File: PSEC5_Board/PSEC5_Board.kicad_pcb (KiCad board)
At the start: 6 copper layers, 76.2 x 76.2 mm, 187 parts, among them IC1 LTC6409IUDB#TRMPBF, IC2 LTC6409IUDB#TRMPBF, IC3 LTC6409IUDB#TRMPBF, IC4 LTC6409IUDB#TRMPBF, IC5 LTC6409IUDB#TRMPBF, IC6 LTC6409IUDB#TRMPBF, IC7 LTC6409IUDB#TRMPBF, IC8 LTC6409IUDB#TRMPBF, J1 QTH-040-01-X-D-DP-A, J11 Conn_Coaxial, J2 Conn_Coaxial, J3 Conn_Coaxial, J4 Conn_Coaxial, J5 Conn_Coaxial, J6 Conn_Coaxial, J7 Conn_Coaxial, J8 Conn_Coaxial, J9 QTH-040-01-X-D-DP-A, U1 MCP1700T-1802E_TT, U3 DAC8411IDCKT, U5 MC100LVEL, U6 OPA607QDBVRQ1, U7 AD4008BCPZ-RL7, Y1 ASE2-40.000MHZ-ET

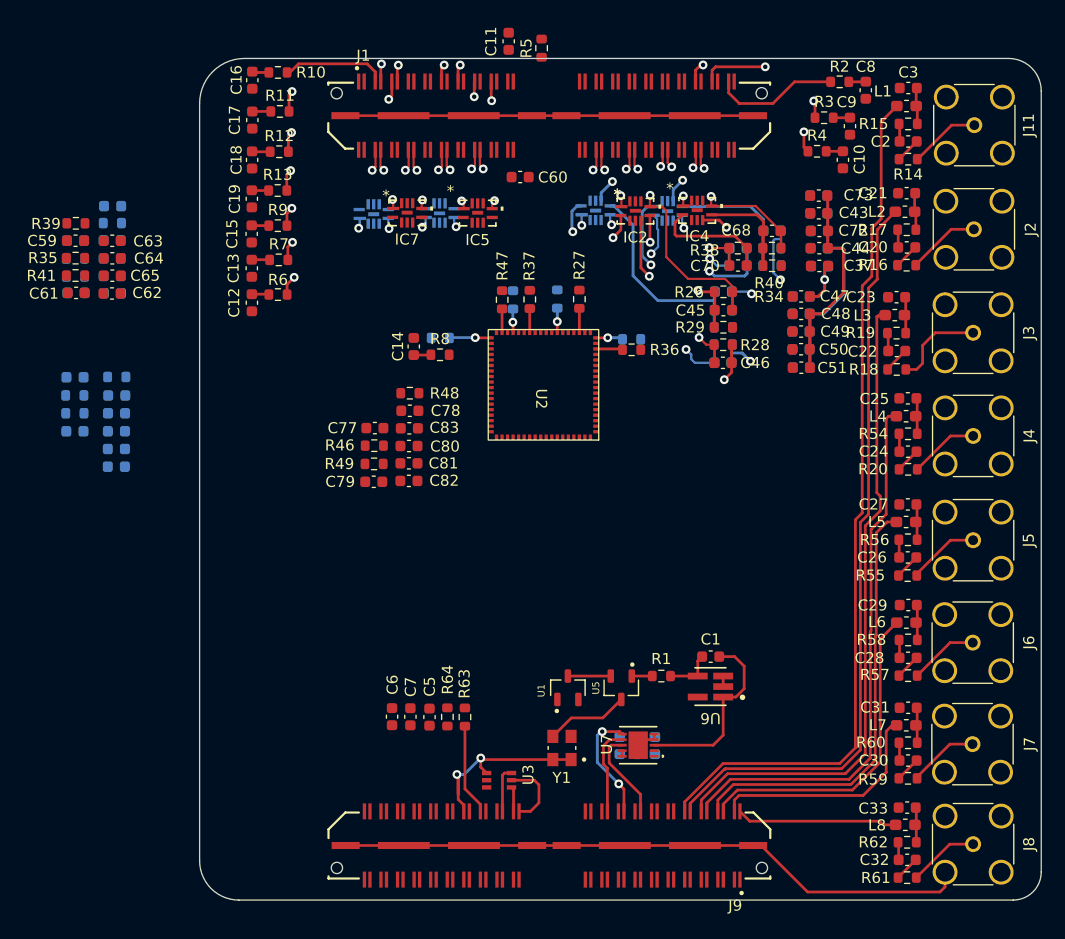
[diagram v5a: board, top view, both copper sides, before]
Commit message: DUT push - All nets
All nets are connected, Power and ground planes not registering.

ERC not completed.
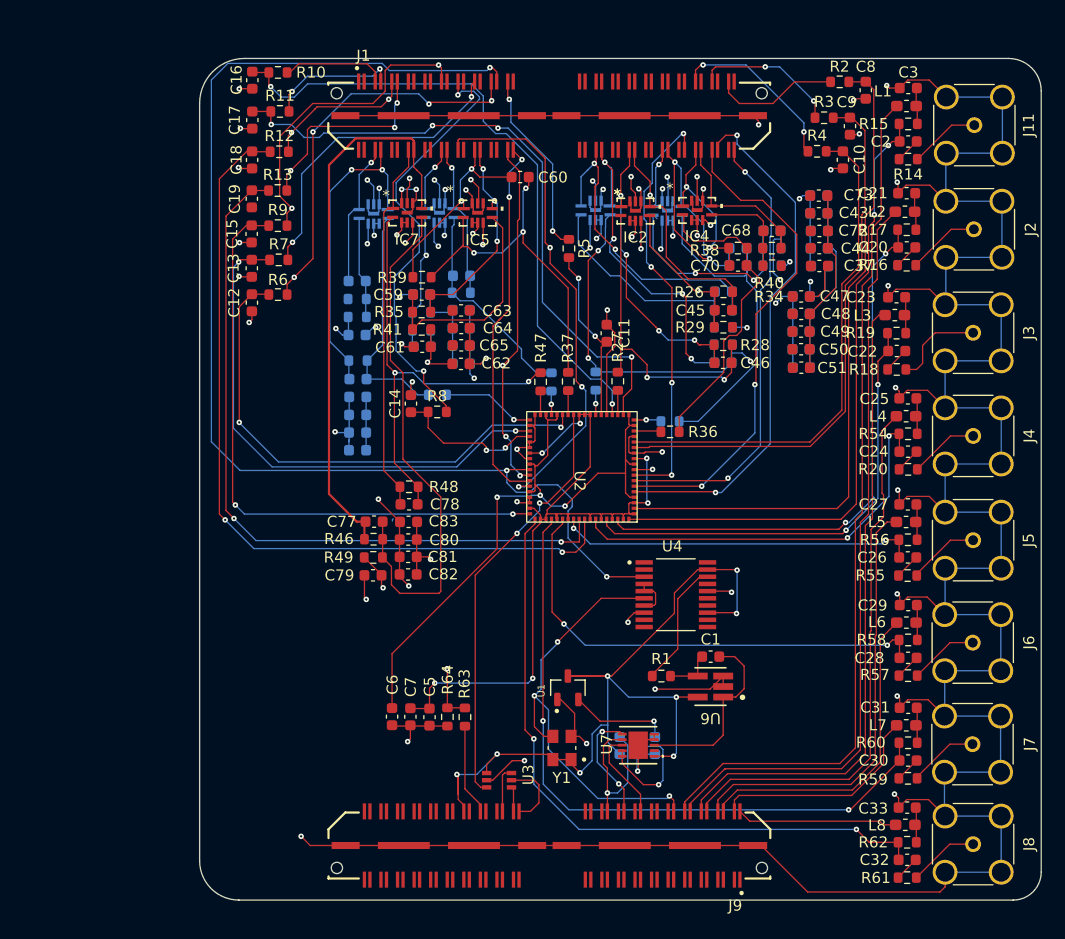
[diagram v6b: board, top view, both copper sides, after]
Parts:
- removed U5: MC100LVEL, MCP1700T_1802E_TT:SOT95P237X112-3N
- added U4: MC100LVEL40DWG, MC100LVEL40DWG:SOP65P640X120-20N, F.Cu at (158.1, 92.4)
- moved C62 32.2 mm to (138.6, 71.5)
- moved C71 32.2 mm to (138.6, 71.5)
- moved C63 32.2 mm to (138.6, 66.6)
- moved C64 32.2 mm to (138.6, 68.2)
- moved C65 32.2 mm to (138.6, 69.8)
- moved C67 32.2 mm to (138.7, 63.5)
- moved C74 32.2 mm to (138.6, 66.6)
- moved C75 32.2 mm to (138.6, 69.8)
- moved C76 32.2 mm to (138.6, 68.2)
- moved R44 32.2 mm to (138.6, 65.0)
- moved C61 31.7 mm to (135.1, 69.9)
- moved C66 31.7 mm to (135.1, 69.9)
- moved R45 31.7 mm to (135.0, 66.8)
- moved C69 31.7 mm to (135.0, 65.2)
- moved R42 31.7 mm to (135.0, 68.4)
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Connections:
- J1 pad 06: ADC8_Out+ -> ADC8_Out-
- J1 pad 08: ADC8_Out- -> ADC8_Out+
- J1 pad 22: ADC6_Out+ -> ADC6_Out-
- J1 pad 24: ADC6_Out- -> ADC6_Out+
- J1 pad 34: rst -> unconnected-(J1-Pad34)
- J1 pad 36: SPIclk -> unconnected-(J1-Pad36)
- J1 pad 46: ADC4_Out+ -> ADC4_Out-
- J1 pad 48: ADC4_Out- -> ADC4_Out+
- J1 pad 62: ADC2_Out+ -> ADC2_Out-
- J1 pad 64: ADC2_Out- -> ADC2_Out+
- J1 pad 74: unconnected-(J1-Pad74) -> rst
- J1 pad 76: unconnected-(J1-Pad76) -> SPIclk
- J9 pad 18: unconnected-(J9-Pad18) -> CLK_OUT
- Y1 pad 3: /Phase_detection/CLK_OUT -> CLK_OUT
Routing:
- net GND: track 97.6 -> 457.9 mm, vias 0 -> 50
- net PSEC5_CLK_OUT: track 0.00 -> 110.7 mm, vias 0 -> 3
- net /Biases,Thresh/wbufbias_postrc: track 1.65 -> 73.0 mm, vias 0 -> 2
- net +1V2: track 0.00 -> 68.6 mm, vias 0 -> 6
- net /Biases,Thresh/discbias_postrc: track 1.53 -> 66.7 mm, vias 0 -> 2
- net /Pedestals/SIGNAL8: track 1.61 -> 61.4 mm, vias 0 -> 2
- net /Pedestals/SIGNAL7: track 1.63 -> 61.0 mm, vias 0 -> 2
- net /Biases,Thresh/discthresh1_postrc: track 1.54 -> 60.2 mm
- net VDD25: track 23.4 -> 81.9 mm, vias 2 -> 8
- net +2V5: track 0.00 -> 57.2 mm, vias 0 -> 3
- net /Biases,Thresh/readbias1_postrc: track 1.53 -> 58.2 mm, vias 0 -> 2
- net /Biases,Thresh/readbias2_postrc: track 1.68 -> 58.0 mm, vias 0 -> 4
- net /Pedestals/SIGNAL1: track 1.61 -> 57.6 mm, vias 0 -> 2
- net VDD33: track 37.9 -> 92.9 mm, vias 0 -> 20
- net /Biases,Thresh/discthresh8_postrc: track 1.56 -> 54.9 mm, vias 0 -> 2
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- added copper zone on In1.Cu, net GND
- added copper zone on In4.Cu, net GND
- added copper zone on In2.Cu, net VDD33
- added copper zone on In3.Cu, net V_OCM

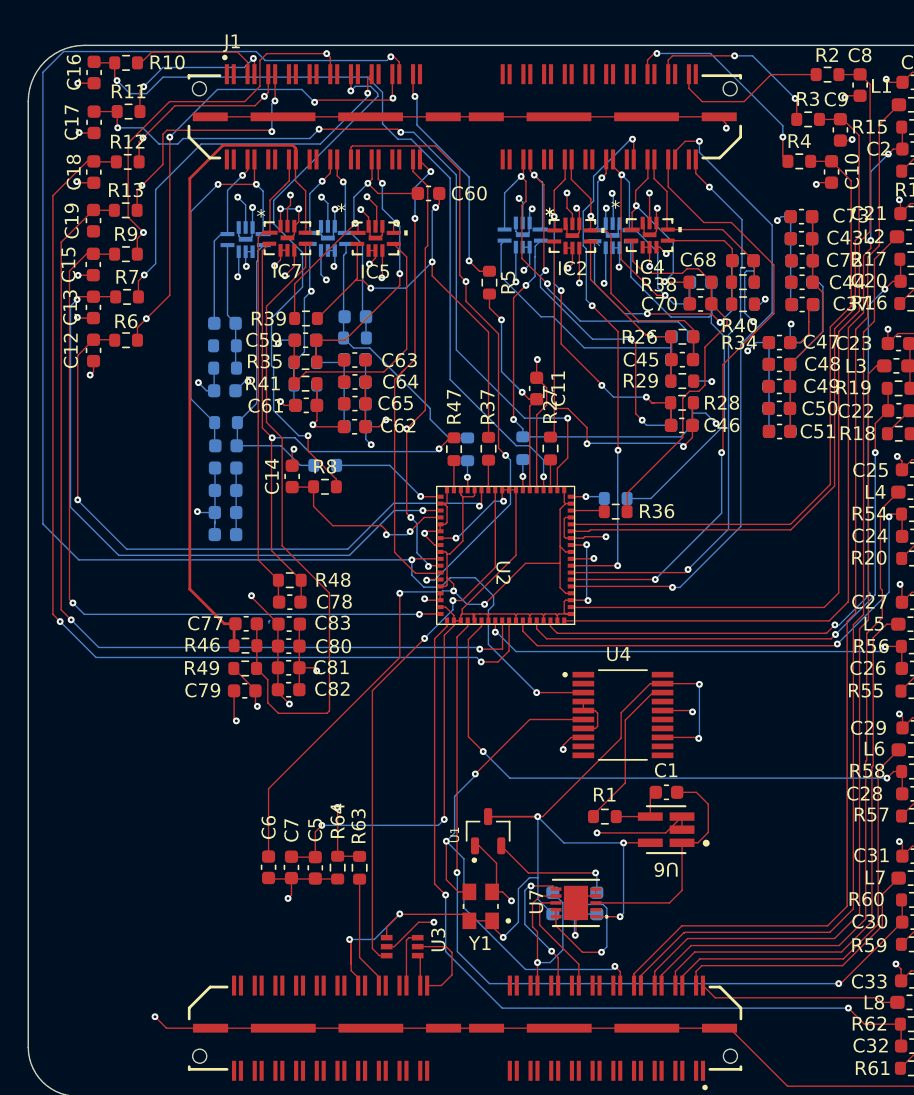
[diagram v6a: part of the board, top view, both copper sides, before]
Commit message: DUT - pre-review: Error free
Ran ERC, no more errors. Cleared most warnings besides silkscreen clipping
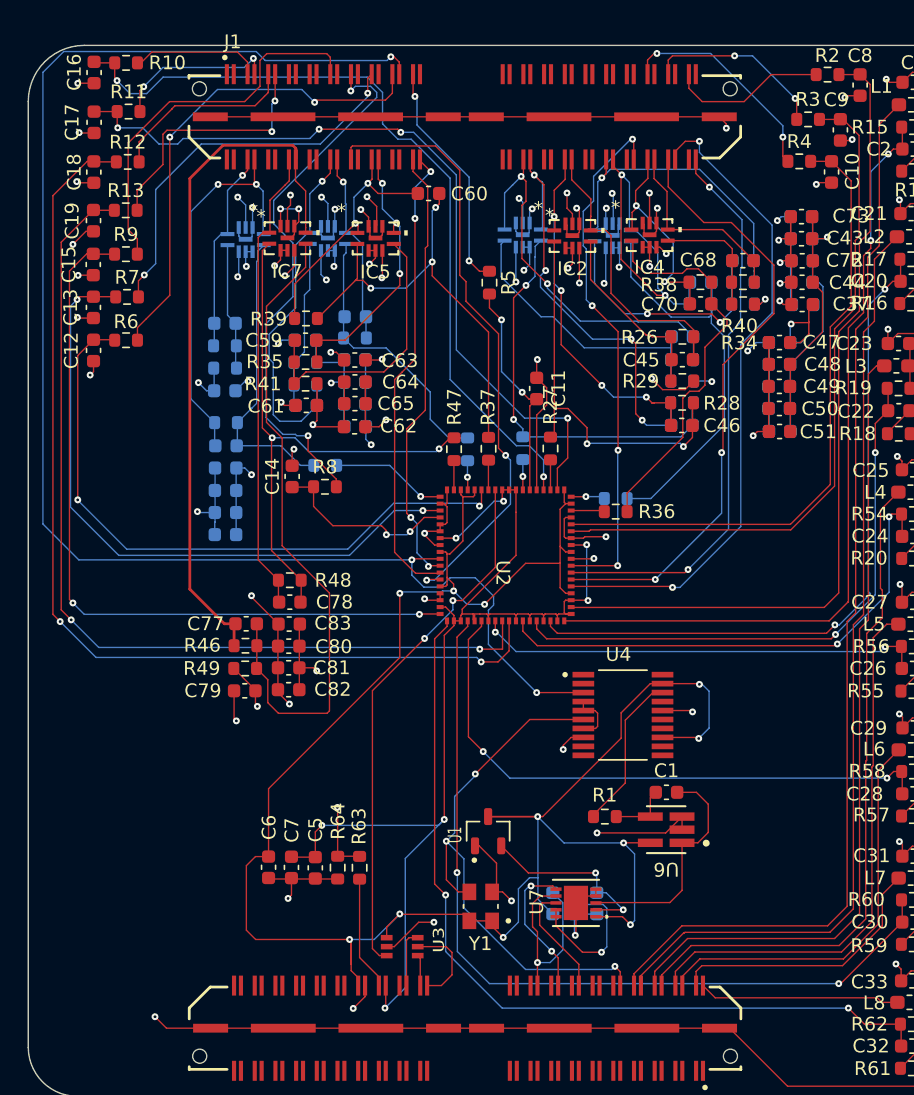
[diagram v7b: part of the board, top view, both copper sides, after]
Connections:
- C5 pad 1: +1V2 -> VDD
- C6 pad 1: +2V5 -> VDD25
- C7 pad 1: +1V2 -> VDD
- U2 pad 10: +2V5 -> VDD25
- U2 pad 12: +1V2 -> VDD
- U2 pad 2: +1V2 -> VDD
- U2 pad 21: +2V5 -> VDD25
- U2 pad 23: +2V5 -> VDD25
- U2 pad 27: +1V2 -> VDD
- U2 pad 28: +1V2 -> VDD
- U2 pad 29: +1V2 -> VDD
- U2 pad 36: +2V5 -> VDD25
- U2 pad 38: +2V5 -> VDD25
- U2 pad 44: +1V2 -> VDD
- U2 pad 45: +2V5 -> VDD25
- U2 pad 5: +2V5 -> VDD25
- U2 pad 51: +2V5 -> VDD25
- U2 pad 52: +1V2 -> VDD
- U2 pad 54: +1V2 -> VDD
- U2 pad 56: +1V2 -> VDD
- U2 pad 58: +1V2 -> VDD
- U2 pad 60: +1V2 -> VDD
- U2 pad 62: +1V2 -> VDD
- U2 pad 66: +1V2 -> VDD
- U2 pad 68: +1V2 -> VDD
- U2 pad 70: +1V2 -> VDD
- U2 pad 71: +1V2 -> VDD
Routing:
- net VDD: track 0.00 -> 85.7 mm, vias 0 -> 7
- net VDD25: track 81.9 -> 156.0 mm, vias 8 -> 11
- net +1V2: track 68.6 -> 0.00 mm, vias 6 -> 0
- net +2V5: track 57.2 -> 0.00 mm, vias 3 -> 0
- net GND: track 457.9 -> 487.4 mm, vias 50 -> 59
- net ADC6_Out-: track 7.46 -> 25.9 mm
- net ADC2_Out-: track 12.2 -> 23.2 mm, vias 2 -> 1
- net VDD33: track 92.9 -> 99.7 mm, vias 20 -> 24
- net Net-(U1-VOUT): track 9.13 -> 13.5 mm, vias 1 -> 2
- net Net-(IC3-+IN): track 31.9 -> 29.9 mm, vias 3 -> 2
- net ADC8_Out-: track 13.2 -> 14.8 mm
- net V_OCM: track 37.2 -> 38.4 mm
- net Net-(IC6-+IN): track 19.3 -> 20.0 mm
- net Disc_Thresh8: track 28.5 -> 28.1 mm, vias 2 -> 0
- net Disc_Thresh5: track 35.6 -> 35.3 mm, vias 4 -> 2
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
